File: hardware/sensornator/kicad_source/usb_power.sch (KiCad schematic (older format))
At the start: 33 parts, among them P1 USB_OTG, Q1 2N7002, Q2 2N7002, Q3 BC847, Q4 BC847, U1 TPS383X, U2 MCP73831, U3 TPS736XX, U4 CP2102N_28

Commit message: changed micro SD card socket to push pull type, updated footprint of micro USB socket
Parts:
- P1: footprint mechanical-connectors:USB_Micro-B -> CON_wuerth:WE_629105136821
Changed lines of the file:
@@
 F 0 "P1" V 1875 1974 50  0000 C CNN
 F 1 "USB_OTG" V 1966 1974 50  0000 C CNN
-F 2 "mechanical-connectors:USB_Micro-B" V 2250 1950 50  0001 C CNN
+F 2 "CON_wuerth:WE_629105136821" V 2250 1950 50  0001 C CNN
 F 3 "" V 2250 1950 50  0000 C CNN
 	1    2300 2050

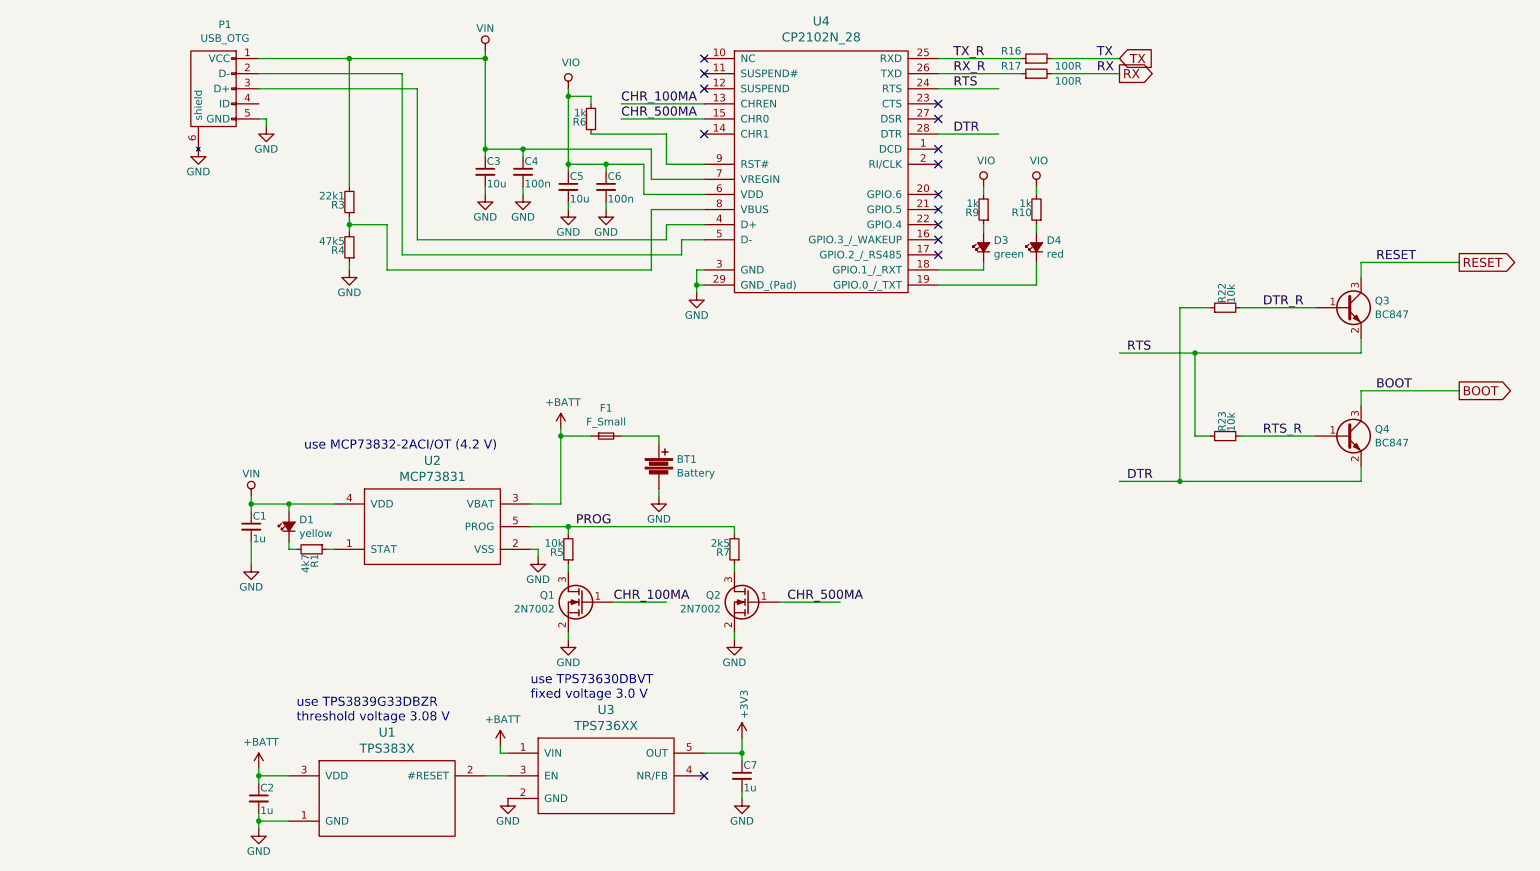
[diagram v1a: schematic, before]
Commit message: updated schematic, added USB voltage bypass, finished layout, corrected 3D models
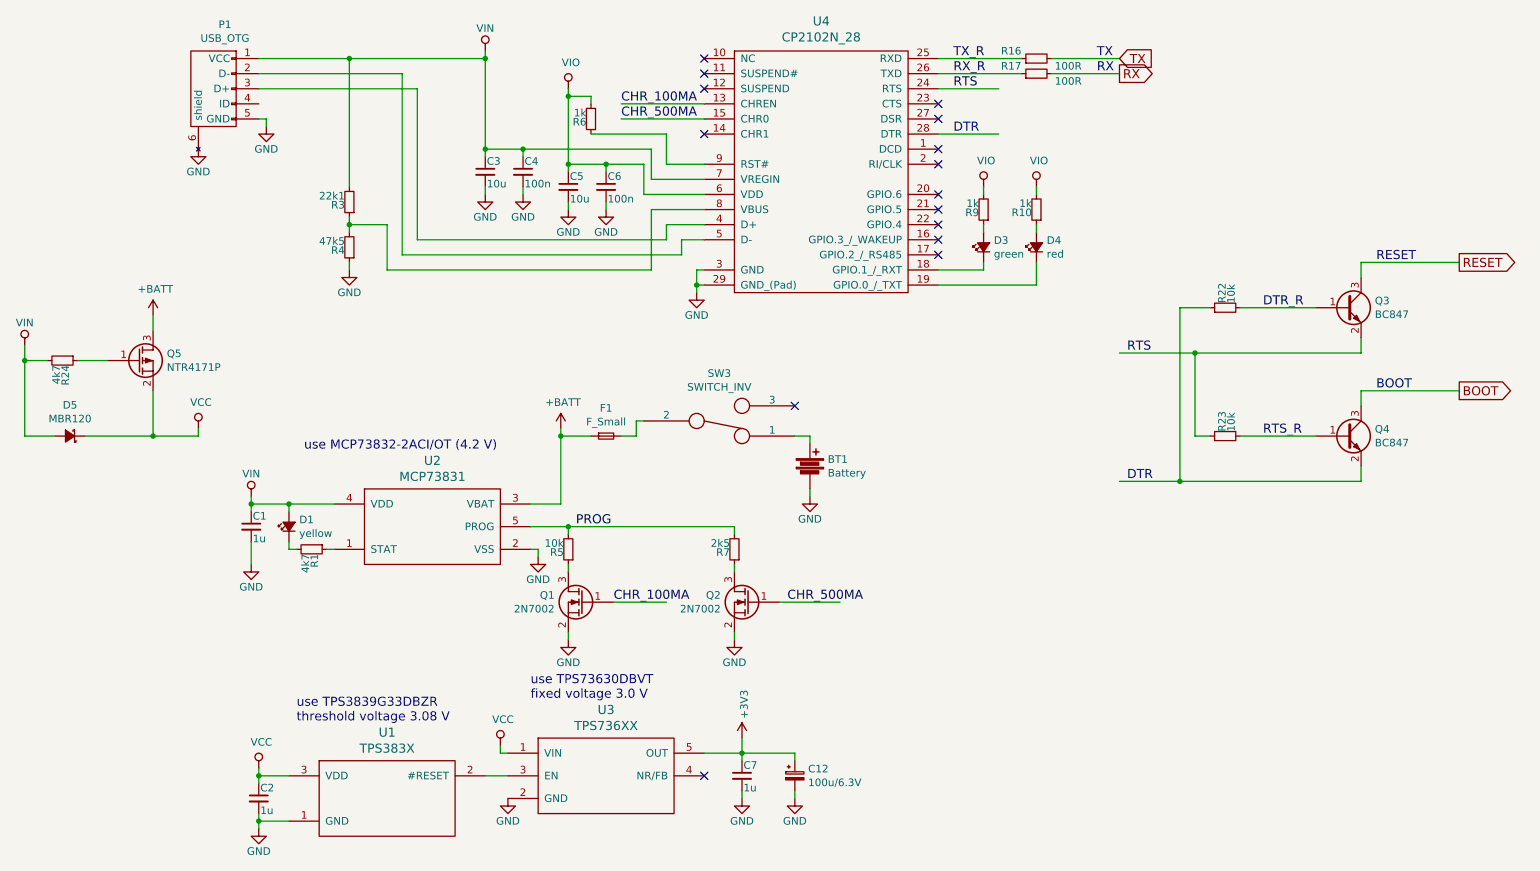
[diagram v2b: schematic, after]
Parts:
- added C12: 100u/6.3V, capacitors:TantalC_SizeD_EIA-7343_Reflow, symbol devices:CP_Small
- added D5: MBR120, diodes:SOD-123, symbol devices:D_Schottky_Small
- added Q5: NTR4171P, SOT_TO:SOT-23, symbol devices:Q_PMOS_GSD
- added R24: 4k7, resistors:R_0603, symbol devices:R_1206
- added SW3: SWITCH_INV, mechanical-switches:WE_450404015514, symbol devices:SWITCH_INV
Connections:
- net labels added: VCC
- wire segments 125 -> 141
- no-connect marks 14 -> 15
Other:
- moved on the sheet: BT1
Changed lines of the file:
@@
 	4200 6450 4200 6400
-$Comp
-L power-supply:+BATT #PWR?
-U 1 1 5CB4F904
-P 4200 6400
-AR Path="/5CB4F904" Ref="#PWR?"  Part="1"
-AR Path="/5CB34EF4/5CB4F904" Ref="#PWR0123"  Part="1"
-F 0 "#PWR0123" H 4200 6250 50  0001 C CNN
-F 1 "+BATT" H 4215 6573 50  0000 C CNN
-F 2 "" H 4200 6400 50  0000 C CNN
-F 3 "" H 4200 6400 50  0000 C CNN
-	1    4200 6400
-	1    0    0    -1
-$EndComp
-$Comp
-L power-supply:+BATT #PWR?
-U 1 1 5CB4F90A
-P 2600 6550
-AR Path="/5CB4F90A" Ref="#PWR?"  Part="1"
-AR Path="/5CB34EF4/5CB4F90A" Ref="#PWR0124"  Part="1"
-F 0 "#PWR0124" H 2600 6400 50  0001 C CNN
-F 1 "+BATT" H 2615 6723 50  0000 C CNN
-F 2 "" H 2600 6550 50  0000 C CNN
-F 3 "" H 2600 6550 50  0000 C CNN
-	1    2600 6550
-	1    0    0    -1
-$EndComp
 $Comp
 L devices:C_0603 C?
@@
 L devices:Battery BT?
 U 1 1 5CB4F961
-P 5250 4550
+P 6250 4550
 AR Path="/5CB4F961" Ref="BT?"  Part="1"
 AR Path="/5CB34EF4/5CB4F961" Ref="BT1"  Part="1"
-F 0 "BT1" H 5368 4596 50  0000 L CNN
-F 1 "Battery" H 5368 4505 50  0000 L CNN
-F 2 "MECH_battery_holder:KEYSTONE_1043" V 5250 4590 50  0001 C CNN
-F 3 "" V 5250 4590 50  0000 C CNN
-	1    5250 4550
+F 0 "BT1" H 6368 4596 50  0000 L CNN
+F 1 "Battery" H 6368 4505 50  0000 L CNN
+F 2 "MECH_battery_holder:KEYSTONE_1043" V 6250 4590 50  0001 C CNN
+F 3 "" V 6250 4590 50  0000 C CNN
+	1    6250 4550
 	1    0    0    -1
 $EndComp
@@
 L power-supply:GND #PWR?
 U 1 1 5CB4F96F
-P 5250 4750
+P 6250 4750
 AR Path="/5CB4F96F" Ref="#PWR?"  Part="1"
 AR Path="/5CB34EF4/5CB4F96F" Ref="#PWR0129"  Part="1"
-F 0 "#PWR0129" H 5250 4500 50  0001 C CNN
-F 1 "GND" H 5250 4600 50  0000 C CNN
-F 2 "" H 5250 4750 50  0000 C CNN
-F 3 "" H 5250 4750 50  0000 C CNN
-	1    5250 4750
+F 0 "#PWR0129" H 6250 4500 50  0001 C CNN
+F 1 "GND" H 6250 4600 50  0000 C CNN
+F 2 "" H 6250 4750 50  0000 C CNN
+F 3 "" H 6250 4750 50  0000 C CNN
+	1    6250 4750
 	1    0    0    -1
 $EndComp
@@
 	4600 4350 4600 4800
 Wire Wire Line
-	5000 4350 5250 4350
-Wire Wire Line
-	5250 4350 5250 4400
-Wire Wire Line
-	5250 4700 5250 4750
+	5000 4350 5100 4350
 Text Label 4700 4950 0    60   ~ 0
 PROG
@@
 Text GLabel 10550 4050 2    60   Output ~ 0
 BOOT
+$Comp
+L devices:CP_Small C12
+U 1 1 5CB11565
+P 6150 6600
+F 0 "C12" H 6238 6646 50  0000 L CNN
+F 1 "100u/6.3V" H 6238 6555 50  0000 L CNN
+F 2 "capacitors:TantalC_SizeD_EIA-7343_Reflow" H 6150 6600 50  0001 C CNN
+F 3 "" H 6150 6600 50  0000 C CNN
+	1    6150 6600
+	1    0    0    -1
+$EndComp
+$Comp
+L power-supply:GND #PWR?
+U 1 1 5CB1174B
+P 6150 6750
+AR Path="/5CB1174B" Ref="#PWR?"  Part="1"
+AR Path="/5CB34EF4/5CB1174B" Ref="#PWR01"  Part="1"
+F 0 "#PWR01" H 6150 6500 50  0001 C CNN
+F 1 "GND" H 6150 6600 50  0000 C CNN
+F 2 "" H 6150 6750 50  0000 C CNN
+F 3 "" H 6150 6750 50  0000 C CNN
+	1    6150 6750
+	1    0    0    -1
+$EndComp
+Wire Wire Line
+	5800 6450 6150 6450
+Wire Wire Line
+	6150 6450 6150 6500
+Wire Wire Line
+	6150 6700 6150 6750
+$Comp
+L devices:SWITCH_INV SW3
+U 1 1 5CB1A0E5
+P 5650 4250
+F 0 "SW3" H 5650 3935 50  0000 C CNN
+F 1 "SWITCH_INV" H 5650 4026 50  0000 C CNN
+F 2 "mechanical-switches:WE_450404015514" H 5650 4250 50  0001 C CNN
+F 3 "" H 5650 4250 50  0000 C CNN
+	1    5650 4250
+	1    0    0    1
+$EndComp
+Wire Wire Line
+	6150 4350 6250 4350
+Wire Wire Line
+	6250 4350 6250 4400
+Wire Wire Line
+	6250 4700 6250 4750
+Wire Wire Line
+	5150 4250 5100 4250
+Wire Wire Line
+	5100 4250 5100 4350
+NoConn ~ 6150 4150
+$Comp
+L devices:Q_PMOS_GSD Q5
+U 1 1 5CB776AF
+P 1800 3850
+F 0 "Q5" H 1991 3896 50  0000 L CNN
+F 1 "NTR4171P" H 1991 3805 50  0000 L CNN
+F 2 "SOT_TO:SOT-23" H 2000 3950 50  0001 C CNN
+F 3 "" H 1800 3850 50  0000 C CNN
+	1    1800 3850
+	1    0    0    -1
+$EndComp
+$Comp
+L power-supply:VIN #PWR?
+U 1 1 5CB7BCC7
+P 1050 3750
+AR Path="/5CB7BCC7" Ref="#PWR?"  Part="1"
+AR Path="/5CB34EF4/5CB7BCC7" Ref="#PWR05"  Part="1"
+F 0 "#PWR05" H 1050 3600 50  0001 C CNN
+F 1 "VIN" H 1050 3900 50  0000 C CNN
+F 2 "" H 1050 3750 50  0000 C CNN
+F 3 "" H 1050 3750 50  0000 C CNN
+	1    1050 3750
+	1    0    0    -1
+$EndComp
+$Comp
+L power-supply:+BATT #PWR?
+U 1 1 5CB7BD67
+P 1900 3550
+AR Path="/5CB7BD67" Ref="#PWR?"  Part="1"
+AR Path="/5CB34EF4/5CB7BD67" Ref="#PWR04"  Part="1"
+F 0 "#PWR04" H 1900 3400 50  0001 C CNN
+F 1 "+BATT" H 1915 3723 50  0000 C CNN
+F 2 "" H 1900 3550 50  0000 C CNN
+F 3 "" H 1900 3550 50  0000 C CNN
+	1    1900 3550
+	1    0    0    -1
+$EndComp
+Wire Wire Line
+	1900 3550 1900 3650
+$Comp
+L power-supply:VCC #PWR06
+U 1 1 5CB896C8
+P 2200 4300
+F 0 "#PWR06" H 2200 4150 50  0001 C CNN
+F 1 "VCC" H 2217 4473 50  0000 C CNN
+F 2 "" H 2200 4300 50  0000 C CNN
+F 3 "" H 2200 4300 50  0000 C CNN
+	1    2200 4300
+	1    0    0    -1
+$EndComp
+$Comp
+L devices:R_1206 R?
+U 1 1 5CB89804
+P 1300 3850
+AR Path="/5CB89804" Ref="R?"  Part="1"
+AR Path="/5CB34EF4/5CB89804" Ref="R24"  Part="1"
+F 0 "R24" H 1330 3870 50  0000 L CNN
+F 1 "4k7" H 1330 3810 50  0000 L CNN
+F 2 "resistors:R_0603" H 1300 3700 50  0001 C CNN
+F 3 "" H 1300 3850 50  0000 C CNN
+	1    1300 3850
+	0    1    1    0
+$EndComp
+Wire Wire Line
+	2200 4300 2200 4350
+Wire Wire Line
+	2200 4350 1900 4350
+Wire Wire Line
+	1900 4350 1900 4050
+Wire Wire Line
+	1600 3850 1400 3850
+Wire Wire Line
+	1200 3850 1050 3850
+Wire Wire Line
+	1050 3850 1050 3750
+$Comp
+L power-supply:VCC #PWR09
+U 1 1 5CB97FF8
+P 2600 6550
+F 0 "#PWR09" H 2600 6400 50  0001 C CNN
+F 1 "VCC" H 2617 6723 50  0000 C CNN
+F 2 "" H 2600 6550 50  0000 C CNN
+F 3 "" H 2600 6550 50  0000 C CNN
+	1    2600 6550
+	1    0    0    -1
+$EndComp
+$Comp
+L power-supply:VCC #PWR08
+U 1 1 5CB98150
+P 4200 6400
+F 0 "#PWR08" H 4200 6250 50  0001 C CNN
+F 1 "VCC" H 4217 6573 50  0000 C CNN
+F 2 "" H 4200 6400 50  0000 C CNN
+F 3 "" H 4200 6400 50  0000 C CNN
+	1    4200 6400
+	1    0    0    -1
+$EndComp
+$Comp
+L devices:D_Schottky_Small D5
+U 1 1 5CB982B9
+P 1350 4350
+F 0 "D5" H 1350 4145 50  0000 C CNN
+F 1 "MBR120" H 1350 4236 50  0000 C CNN
+F 2 "diodes:SOD-123" V 1350 4350 50  0001 C CNN
+F 3 "" V 1350 4350 50  0000 C CNN
+	1    1350 4350
+	-1   0    0    1
+$EndComp
+Wire Wire Line
+	1450 4350 1900 4350
+Connection ~ 1900 4350
+Wire Wire Line
+	1250 4350 1050 4350
+Wire Wire Line
+	1050 4350 1050 3850
+Connection ~ 1050 3850
 $EndSCHEMATC

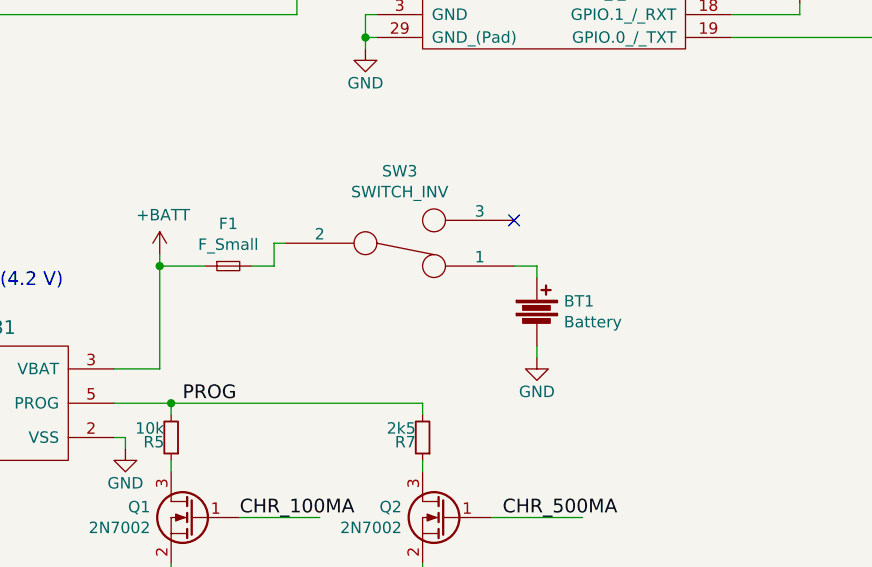
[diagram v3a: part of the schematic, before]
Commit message: added some part values
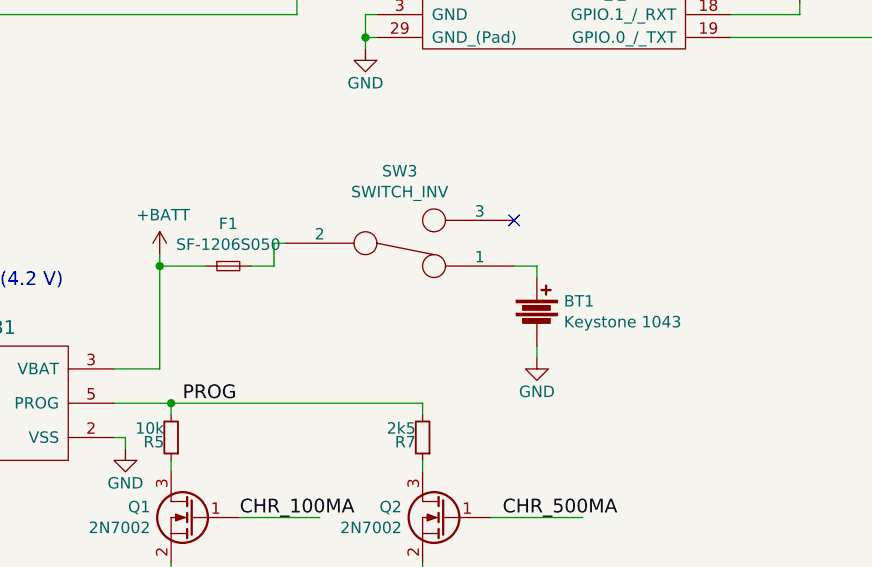
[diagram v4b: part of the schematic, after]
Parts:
- BT1: value Battery -> Keystone 1043
- F1: value F_Small -> SF-1206S050
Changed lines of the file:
@@
 AR Path="/5CB34EF4/5CB4F961" Ref="BT1"  Part="1"
 F 0 "BT1" H 6368 4596 50  0000 L CNN
-F 1 "Battery" H 6368 4505 50  0000 L CNN
+F 1 "Keystone 1043" H 6368 4505 50  0000 L CNN
 F 2 "MECH_battery_holder:KEYSTONE_1043" V 6250 4590 50  0001 C CNN
 F 3 "" V 6250 4590 50  0000 C CNN
@@
 AR Path="/5CB34EF4/5CB4F968" Ref="F1"  Part="1"
 F 0 "F1" H 4900 4535 50  0000 C CNN
-F 1 "F_Small" H 4900 4444 50  0000 C CNN
+F 1 "SF-1206S050" H 4900 4444 50  0000 C CNN
 F 2 "fuse_holders_and_fuses:Fuse_SMD1206_Reflow" H 4900 4350 50  0001 C CNN
 F 3 "" H 4900 4350 50  0000 C CNN
